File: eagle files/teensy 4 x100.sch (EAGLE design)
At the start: 57 parts, among them IC2 LTV846S, IC3 LTV846S, IC4 74AHCT541A, IC5 74AHCT541A, IC6 LM358D, IC7 ULN2003AD

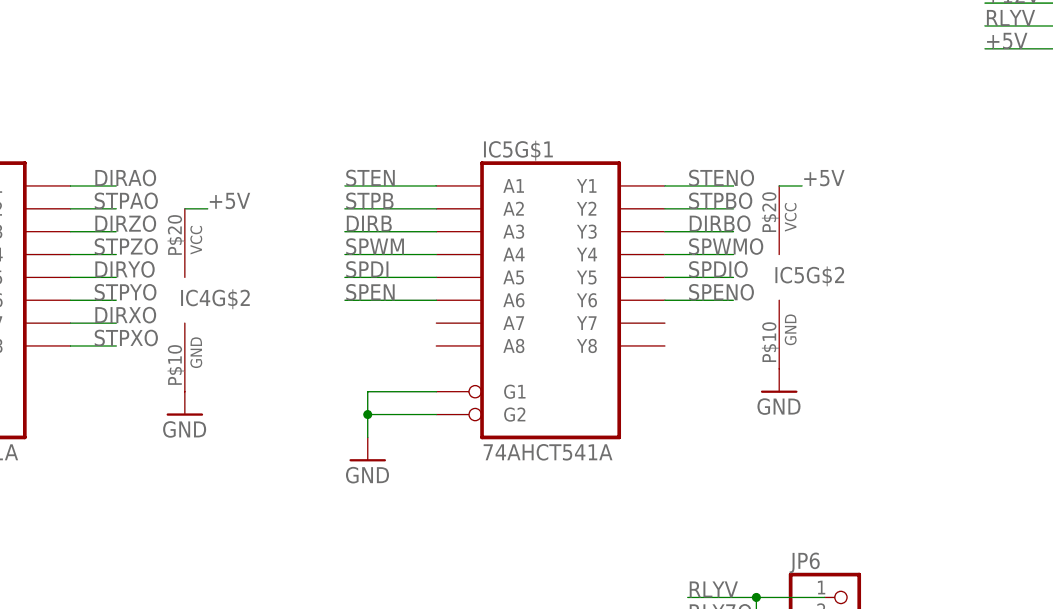
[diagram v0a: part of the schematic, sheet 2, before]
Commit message: Add files via upload
fix to stepper enable lines
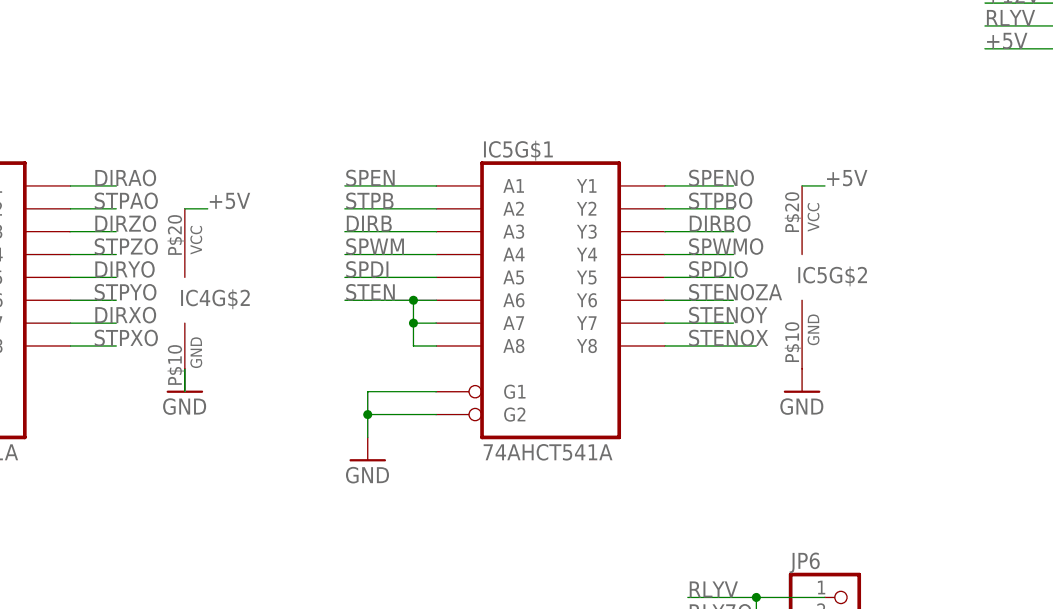
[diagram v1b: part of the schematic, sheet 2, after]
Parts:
- IC1: value (none) -> 24LCxxx
- JP6: device pinhead:PINHD-1X6 -> phils connectors:PINHD-1X6
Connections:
- removed net STENO: IC5G$1.Y1, JP1.4, JP2.4, JP4.4, JP8.4, TR11.1, TR12.1, TR13.1, TR20.1
- new net STENOX: IC5G$1.Y8, JP1.4, TR11.1
- new net STENOY: IC5G$1.Y7, JP2.4, TR12.1
- new net STENOZA: IC5G$1.Y6, JP4.4, JP8.4, TR13.1, TR20.1
- net SPEN: now also IC5G$1.A1; no longer IC5G$1.A6
- net SPENO: now also IC5G$1.Y1; no longer IC5G$1.Y6
- net STEN: now also IC5G$1.A6, IC5G$1.A7, IC5G$1.A8; no longer IC5G$1.A1
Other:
- moved on the sheet: IC5G$2

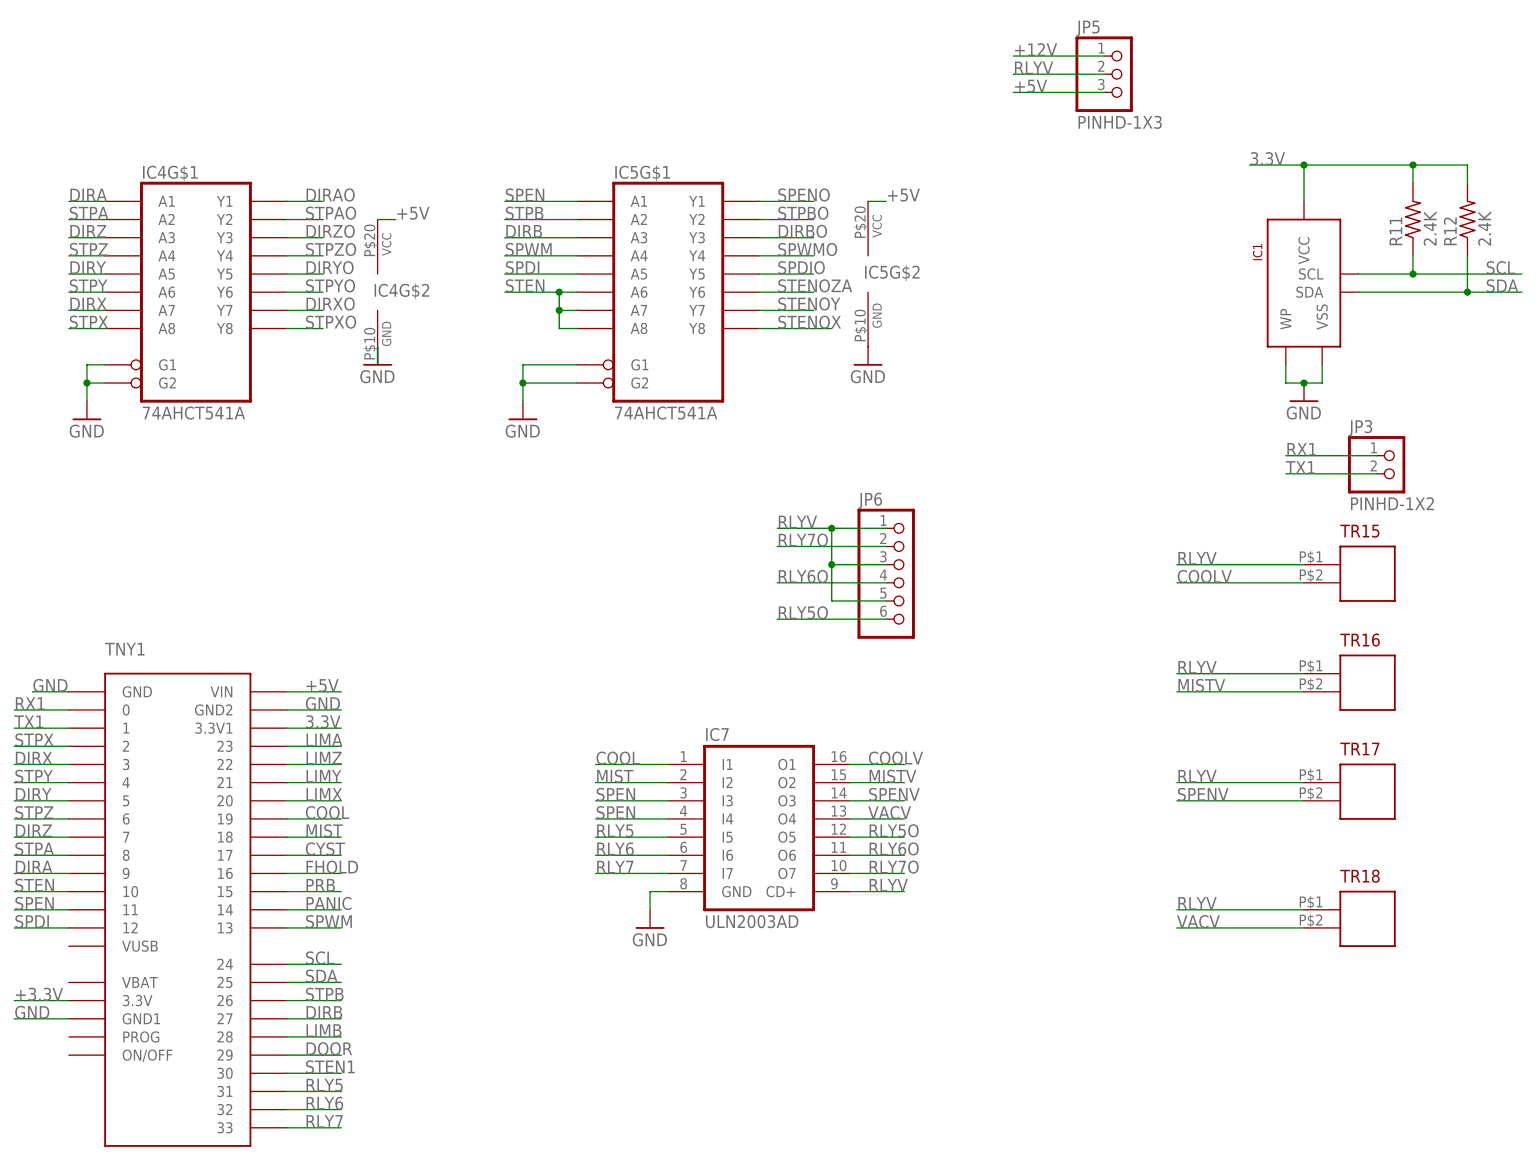
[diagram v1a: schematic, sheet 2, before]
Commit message: Add files via upload
Added i2c header, trace clean up.
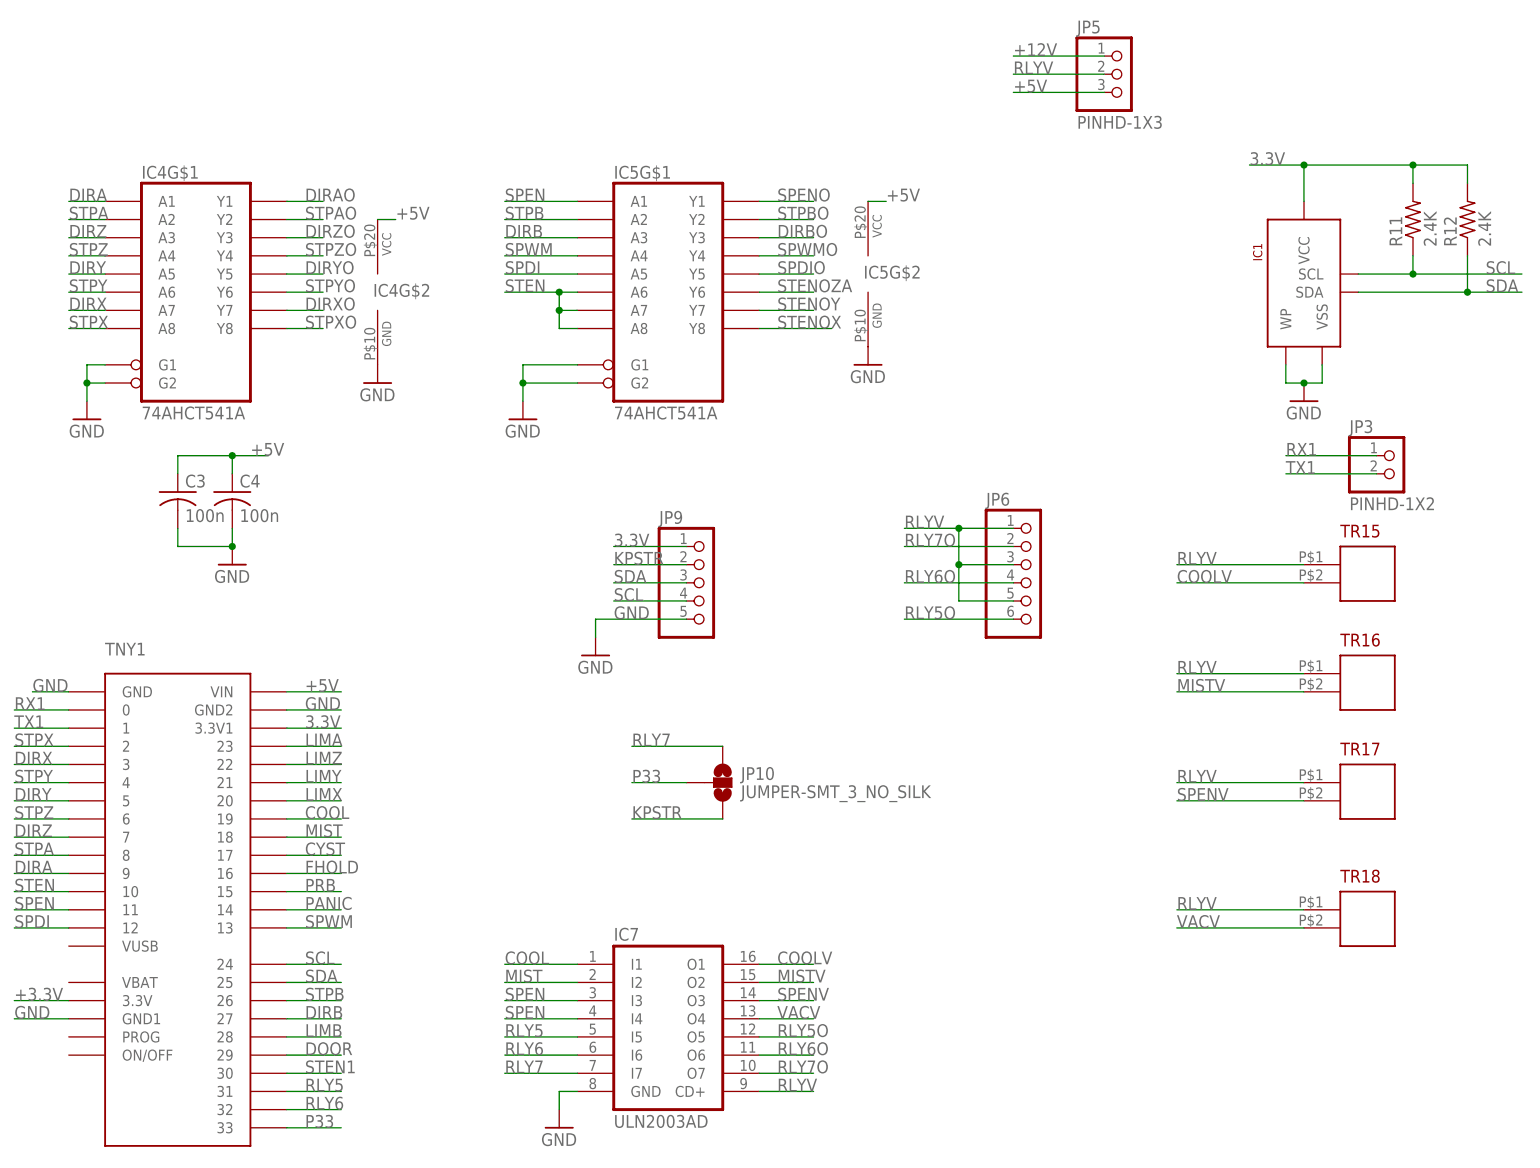
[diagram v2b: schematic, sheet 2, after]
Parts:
- added C3, C4: 100n, rcl:C-USC1206
- added JP10: JUMPER-SMT_3_NO_SILK, phils connectors:JUMPER-SMT_3_NO_SILK
- added JP9: (no value), phils connectors:PINHD-1X5
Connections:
- new net KPSTR: JP10.3, JP9.2
- new net P33: JP10.2, TNY1.33
- net +5V: now also C3.1, C4.1
- net 3.3V: now also JP9.1
- net GND: now also C3.2, C4.2, JP9.5
- net RLY7: now also JP10.1; no longer TNY1.33
- net SCL: now also JP9.4
- net SDA: now also JP9.3
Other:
- moved on the sheet: IC7, JP6

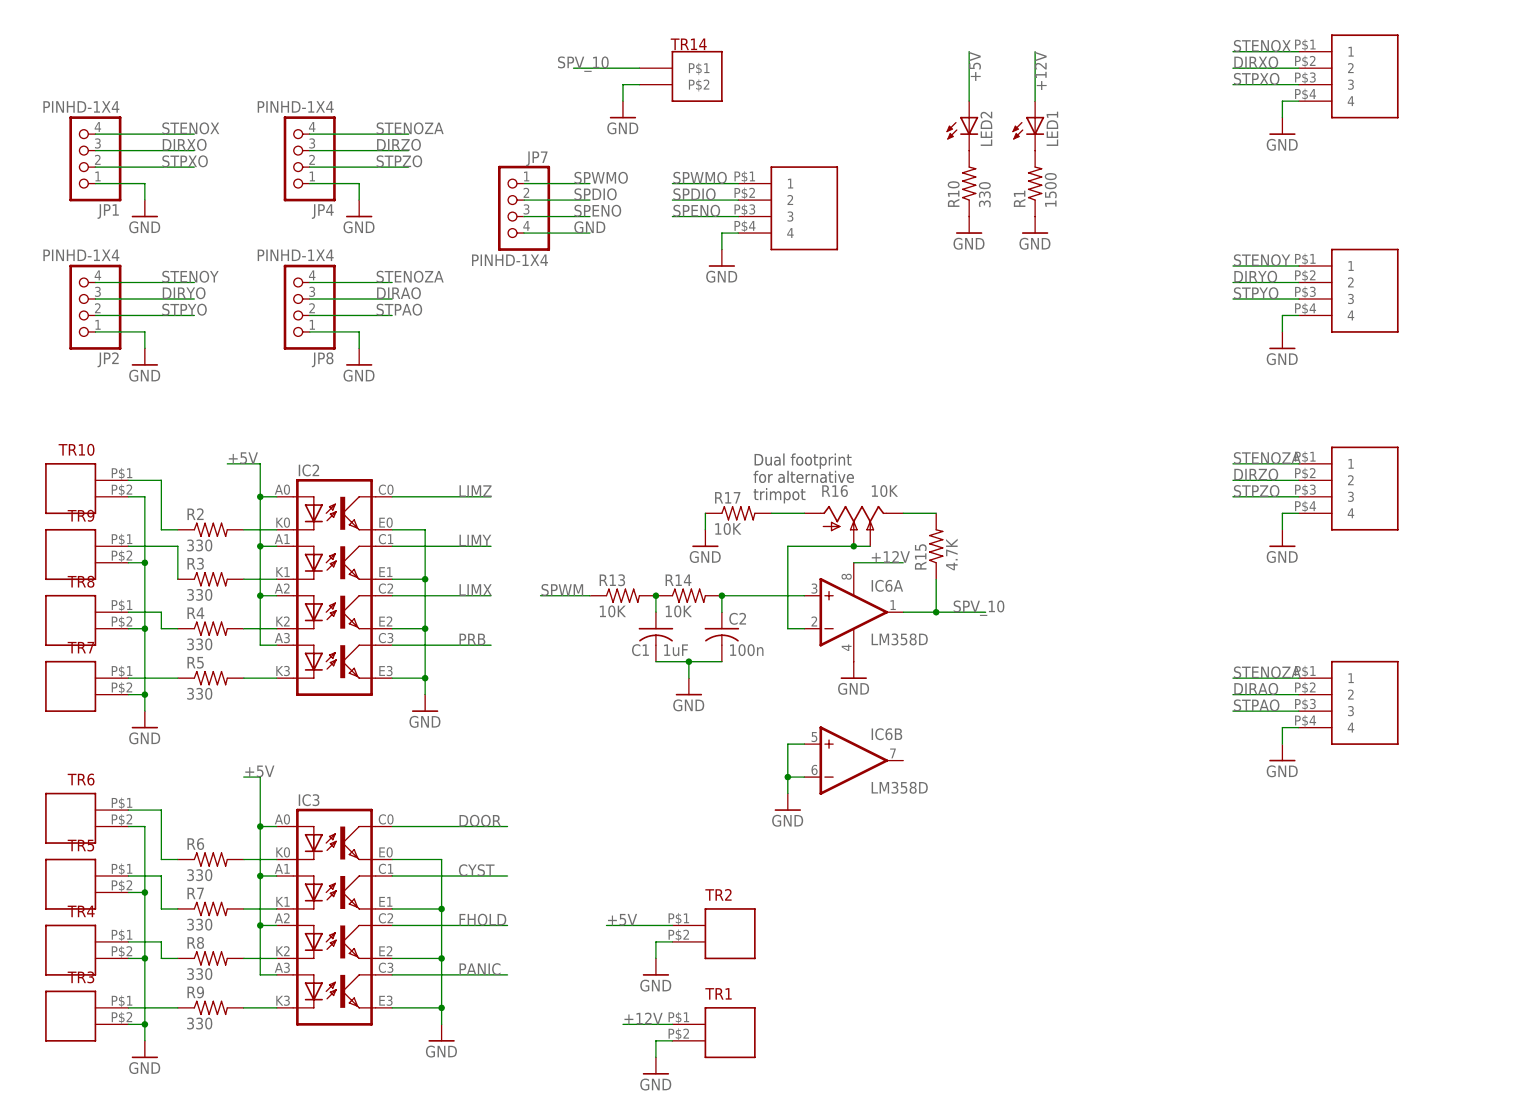
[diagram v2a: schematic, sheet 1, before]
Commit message: Add files via upload
Changed spindle pin assignments, in line with the Teensy 4 Pinouts PDF
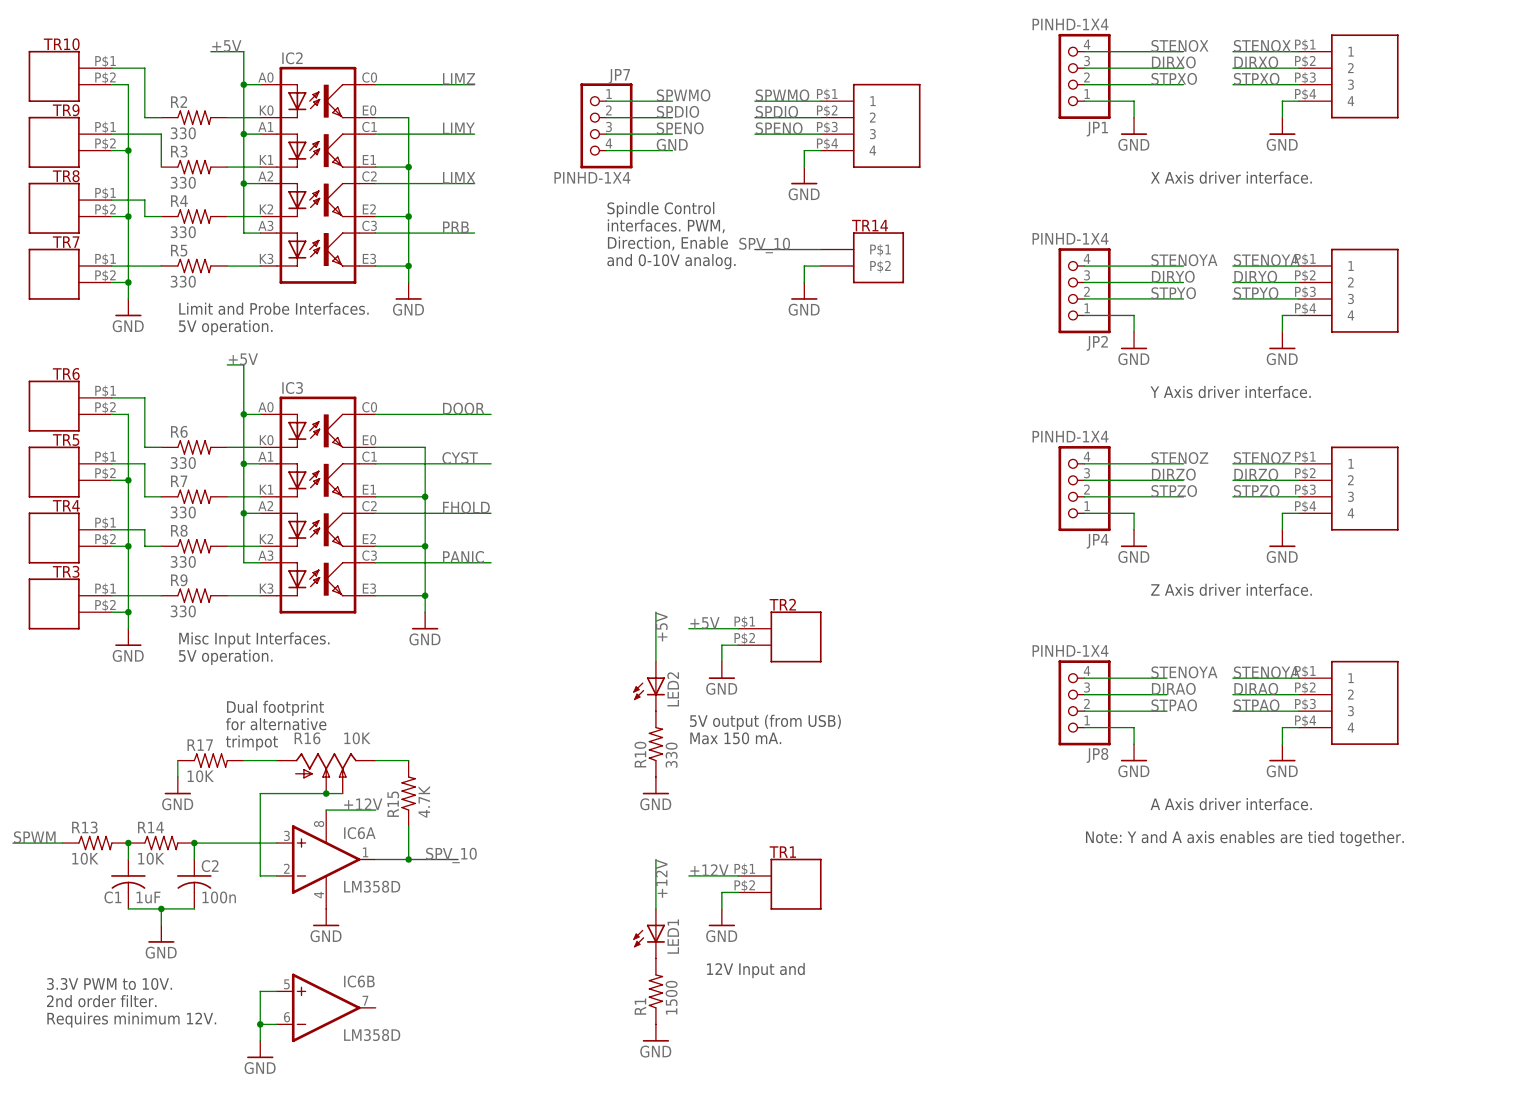
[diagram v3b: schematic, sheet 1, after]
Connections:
- removed net STENOY: IC5G$1.Y7, JP2.4, TR12.1
- removed net STENOZA: IC5G$1.Y6, JP4.4, JP8.4, TR13.1, TR20.1
- new net STENOYA: IC5G$1.Y7, JP2.4, JP8.4, TR12.1, TR20.1
- new net STENOZ: IC5G$1.Y6, JP4.4, TR13.1
- net SPDI: now also TNY1.11; no longer TNY1.12
- net SPEN: now also TNY1.12; no longer TNY1.11
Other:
- note added: "12V Input and"
- note added: "3.3V PWM to 10V. 2nd order filter. Requires minimum 12V."
- note added: "5V output (from USB) Max 150 mA."
- note added: "74 logic bypass caps, necessary?"
- note added: "A Axis driver interface."
- note added: "Additional relays. Pin header only."
- note added: "Aux Relays"
- note added: "EEPROM"
- note added: "External Opto Drivers"
- note added: "I2C Header"
- note added: "I2C Strobe Relay 7 switch"
- note added: "I2C interface tied to 3rd channel on Teensy 4. Extra line mpx'd with relay 7."
- note added: "Limit and Probe Interfaces. 5V operation."
- note added: "Misc Input Interfaces. 5V operation."
- note added: "Note: Y and A axis enables are tied together."
- note added: "Relay Drivers"
- note added: "Relay Power Jumper"
- note added: "Relay Screw Terminals"
- note added: "Serial 1 from Teensy for external USB interface."
- note added: "Spindle Control interfaces. PWM, Direction, Enable and 0-10V analog."
- note added: "X Axis driver interface."
- note added: "Y Axis driver interface."
- note added: "Z Axis driver interface."
- moved on the sheet: C1, C2, IC1, IC2, IC3, IC4G$1, IC4G$2, IC5G$1, IC5G$2, IC6A, IC6B, JP1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
